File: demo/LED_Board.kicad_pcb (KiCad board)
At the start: 2 copper layers, 40 x 16 mm, 5 parts, among them J4 Conn_01x02_Male, J5 Conn_01x02_Male

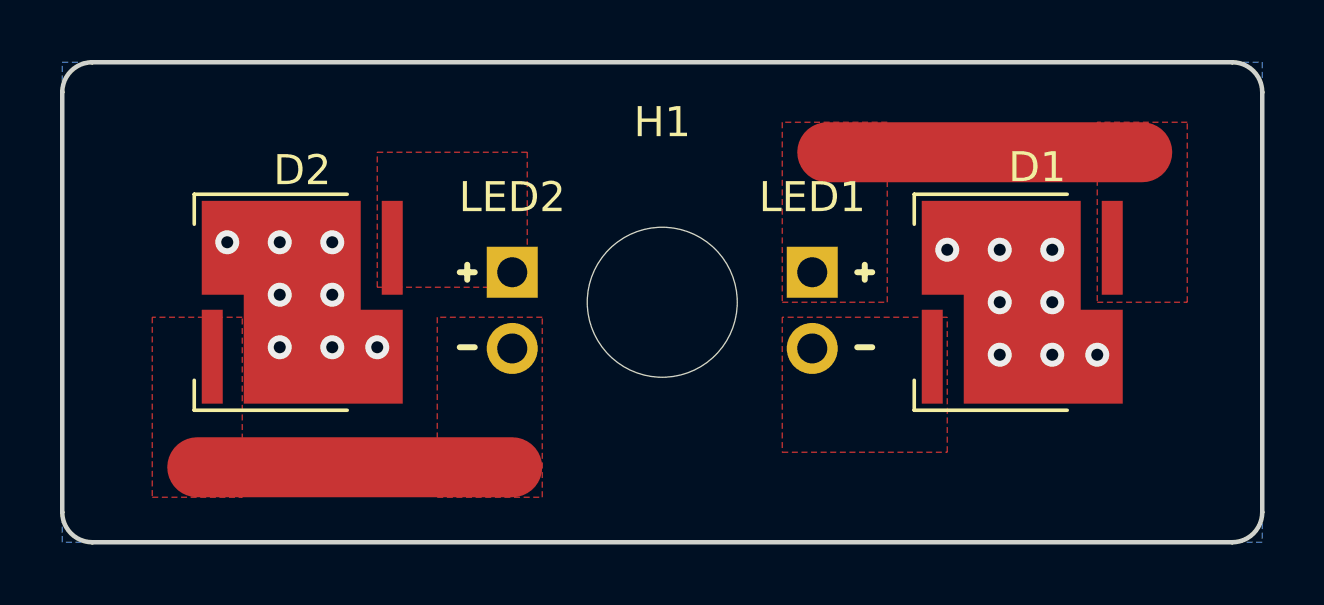
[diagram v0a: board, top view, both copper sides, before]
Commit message: Закончена разводка платы
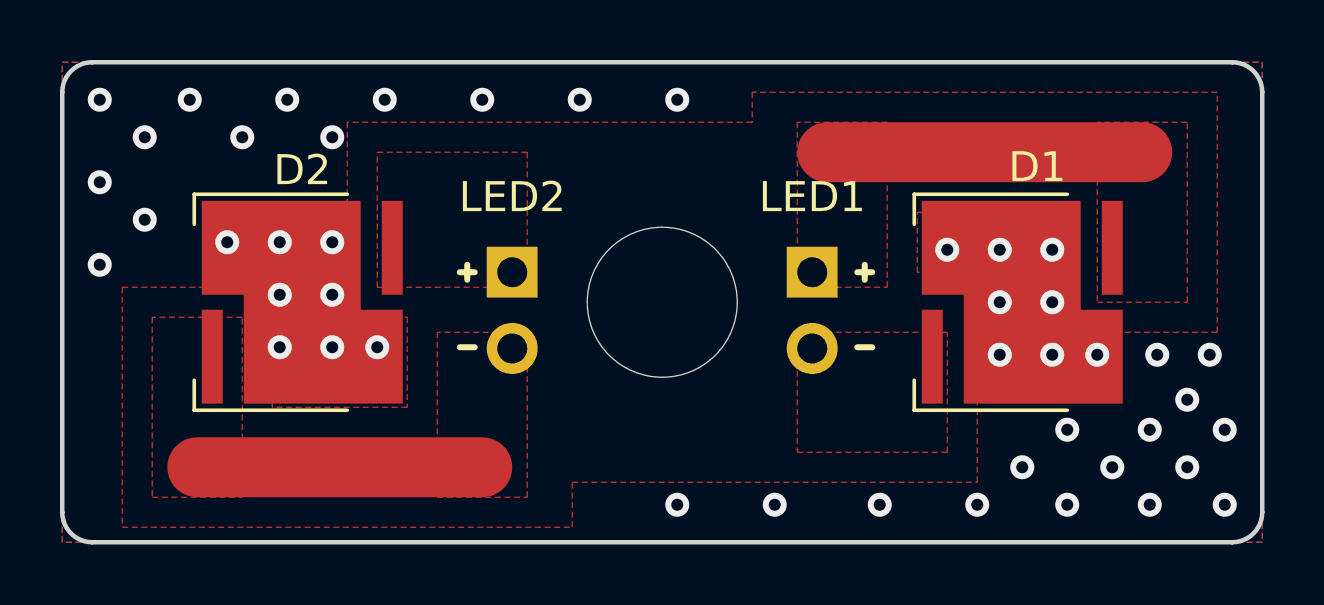
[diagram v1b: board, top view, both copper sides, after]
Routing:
- net /LED2-: track 10.5 -> 9.50 mm
- net /T: vias 16 -> 45
- added copper zone on F.Cu, net /T
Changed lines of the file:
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@@
     (thickness 1.6)
     (drawings 20)
-    (tracks 18)
+    (tracks 47)
     (zones 0)
     (modules 5)
@@
     (last_trace_width 2)
     (trace_clearance 0.5)
-    (zone_clearance 0.8)
+    (zone_clearance 0.5)
     (zone_45_only no)
     (trace_min 0.2)
@@
     (tags "mounting hole 5mm no annular")
     (attr virtual)
-    (fp_text reference H1 (at 0 -6) (layer F.SilkS)
+    (fp_text reference H1 (at 0 -6) (layer F.SilkS) hide
       (effects (font (size 1 1) (thickness 0.15)))
     )
@@
   (gr_line (start 99.5 66) (end 99.5 52) (layer Edge.Cuts) (width 0.15))
   (gr_line (start 139.5 52) (end 139.5 66) (layer Edge.Cuts) (width 0.15))
+  (segment (start 125 54) (end 135.5 54) (width 2) (layer F.Cu) (net 2))
   (via (at 132.5 59) (size 0.8) (drill 0.4) (layers F.Cu B.Cu) (net 3))
   (via (at 130.75 59) (size 0.8) (drill 0.4) (layers F.Cu B.Cu) (net 3))
@@
   (via (at 106.75 57) (size 0.8) (drill 0.4) (layers F.Cu B.Cu) (net 3))
   (via (at 105 57) (size 0.8) (drill 0.4) (layers F.Cu B.Cu) (net 3))
-  (segment (start 114.5 64.5) (end 104 64.5) (width 2) (layer F.Cu) (net 4))
-  (segment (start 125 54) (end 135.5 54) (width 2) (layer F.Cu) (net 2))
   (via (at 130.75 60.75) (size 0.8) (drill 0.4) (layers F.Cu B.Cu) (net 3))
   (via (at 132.5 60.75) (size 0.8) (drill 0.4) (layers F.Cu B.Cu) (net 3))
   (via (at 134 60.75) (size 0.8) (drill 0.4) (layers F.Cu B.Cu) (net 3))
+  (via (at 136 60.75) (size 0.8) (drill 0.4) (layers F.Cu B.Cu) (net 3))
+  (via (at 137.75 60.75) (size 0.8) (drill 0.4) (layers F.Cu B.Cu) (net 3))
+  (via (at 137 62.25) (size 0.8) (drill 0.4) (layers F.Cu B.Cu) (net 3))
+  (via (at 135.75 63.25) (size 0.8) (drill 0.4) (layers F.Cu B.Cu) (net 3))
+  (via (at 138.25 63.25) (size 0.8) (drill 0.4) (layers F.Cu B.Cu) (net 3))
+  (via (at 137 64.5) (size 0.8) (drill 0.4) (layers F.Cu B.Cu) (net 3))
+  (via (at 138.25 65.75) (size 0.8) (drill 0.4) (layers F.Cu B.Cu) (net 3))
+  (via (at 135.75 65.75) (size 0.8) (drill 0.4) (layers F.Cu B.Cu) (net 3))
+  (via (at 134.5 64.5) (size 0.8) (drill 0.4) (layers F.Cu B.Cu) (net 3))
+  (via (at 133 65.75) (size 0.8) (drill 0.4) (layers F.Cu B.Cu) (net 3))
+  (via (at 131.5 64.5) (size 0.8) (drill 0.4) (layers F.Cu B.Cu) (net 3))
+  (via (at 130 65.75) (size 0.8) (drill 0.4) (layers F.Cu B.Cu) (net 3))
+  (via (at 133 63.25) (size 0.8) (drill 0.4) (layers F.Cu B.Cu) (net 3))
+  (via (at 126.75 65.75) (size 0.8) (drill 0.4) (layers F.Cu B.Cu) (net 3))
+  (via (at 123.25 65.75) (size 0.8) (drill 0.4) (layers F.Cu B.Cu) (net 3))
+  (via (at 120 65.75) (size 0.8) (drill 0.4) (layers F.Cu B.Cu) (net 3))
+  (via (at 100.75 52.25) (size 0.8) (drill 0.4) (layers F.Cu B.Cu) (net 3))
+  (via (at 103.75 52.25) (size 0.8) (drill 0.4) (layers F.Cu B.Cu) (net 3))
+  (via (at 107 52.25) (size 0.8) (drill 0.4) (layers F.Cu B.Cu) (net 3))
+  (via (at 110.25 52.25) (size 0.8) (drill 0.4) (layers F.Cu B.Cu) (net 3))
+  (via (at 113.5 52.25) (size 0.8) (drill 0.4) (layers F.Cu B.Cu) (net 3))
+  (via (at 116.75 52.25) (size 0.8) (drill 0.4) (layers F.Cu B.Cu) (net 3))
+  (via (at 120 52.25) (size 0.8) (drill 0.4) (layers F.Cu B.Cu) (net 3))
+  (via (at 102.25 53.5) (size 0.8) (drill 0.4) (layers F.Cu B.Cu) (net 3))
+  (via (at 105.5 53.5) (size 0.8) (drill 0.4) (layers F.Cu B.Cu) (net 3))
+  (via (at 108.5 53.5) (size 0.8) (drill 0.4) (layers F.Cu B.Cu) (net 3))
+  (via (at 100.75 55) (size 0.8) (drill 0.4) (layers F.Cu B.Cu) (net 3))
+  (via (at 102.25 56.25) (size 0.8) (drill 0.4) (layers F.Cu B.Cu) (net 3))
+  (via (at 100.75 57.75) (size 0.8) (drill 0.4) (layers F.Cu B.Cu) (net 3))
+  (segment (start 113.5 64.5) (end 104 64.5) (width 2) (layer F.Cu) (net 4))
   (zone (net 5) (net_name /LED2+) (layer F.Cu) (hatch edge 0.508)
     (connect_pads (clearance 0.8))
@@
     (polygon
       (pts
-        (xy 123.5 59) (xy 127 59) (xy 127 53) (xy 123.5 53)
+        (xy 124 58.5) (xy 127 58.5) (xy 127 53) (xy 124 53)
       )
     )
@@
     (polygon
       (pts
-        (xy 123.5 64) (xy 129 64) (xy 129 59.5) (xy 123.5 59.5)
+        (xy 124 64) (xy 129 64) (xy 129 60) (xy 124 60)
       )
     )
@@
     (polygon
       (pts
-        (xy 115.5 59.5) (xy 112 59.5) (xy 112 65.5) (xy 115.5 65.5)
+        (xy 115 60) (xy 112 60) (xy 112 65.5) (xy 115 65.5)
       )
     )
@@
       )
     )
+  )
+  (zone (net 3) (net_name /T) (layer F.Cu) (hatch edge 0.508)
+    (connect_pads (clearance 0.5))
+    (min_thickness 0.25)
+    (fill yes (arc_segments 16) (thermal_gap 0.5) (thermal_bridge_width 2))
+    (polygon
+      (pts
+        (xy 139.5 67) (xy 99.5 67) (xy 99.5 59) (xy 99.5 51) (xy 139.5 51)
+      )
+    )
+    (polygon
+      (pts
+        (xy 116.5 66.5) (xy 116.5 65) (xy 130 65) (xy 130 58) (xy 128 58)
+        (xy 128 56) (xy 133 56) (xy 133 60) (xy 138 60) (xy 138 52)
+        (xy 122.5 52) (xy 122.5 53) (xy 109 53) (xy 109 59.5) (xy 111 59.5)
+        (xy 111 62.5) (xy 106.5 62.5) (xy 106.5 58.5) (xy 101.5 58.5) (xy 101.5 66.5)
+      )
+    )
